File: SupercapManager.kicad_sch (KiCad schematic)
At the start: 9 parts, among them J1 JST4_F, J2 XT30_F, J3 XT30_F, J4 XT30_F, J5 XT30_F, Q11 BSC059N04LS6, Q12 BSC059N04LS6

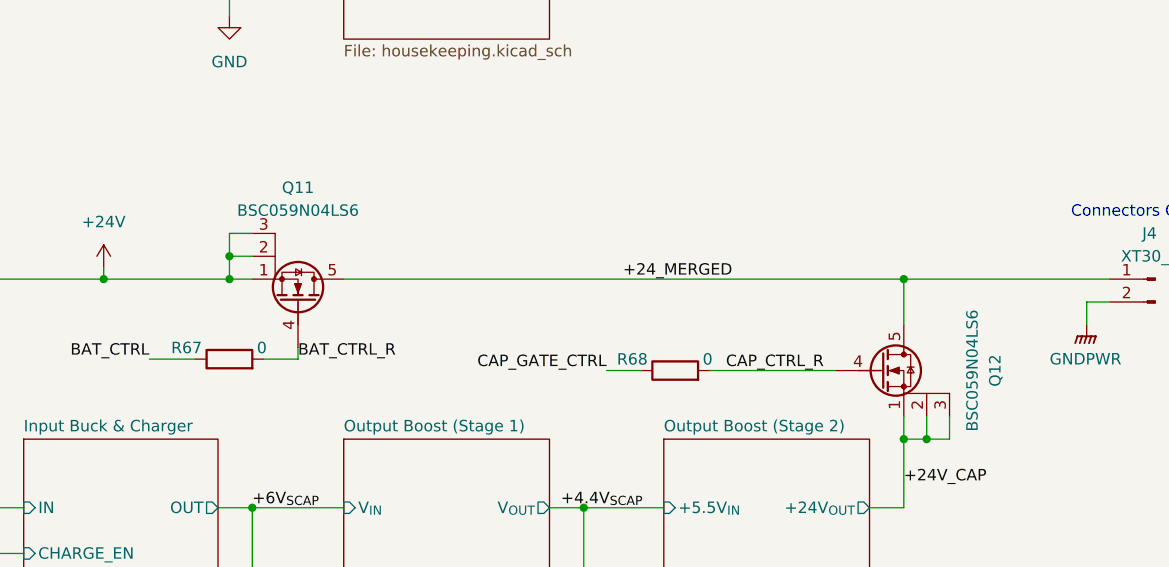
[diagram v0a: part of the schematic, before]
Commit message: Reannotate schematic
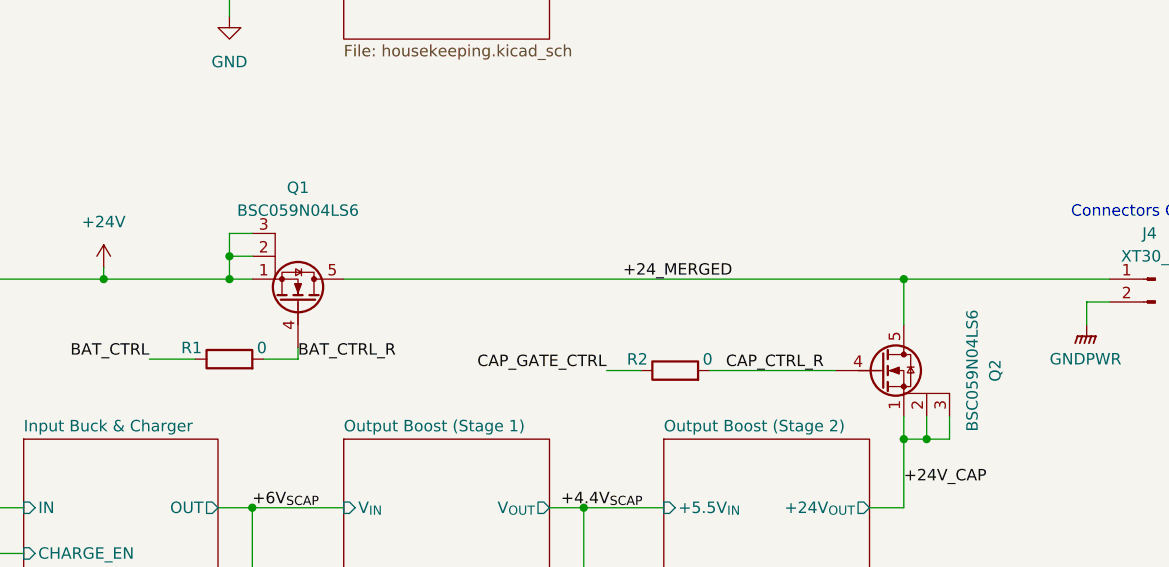
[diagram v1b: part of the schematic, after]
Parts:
- renumbered Q11 to Q1, Q12 to Q2, R67 to R1, R68 to R2
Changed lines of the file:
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@@
 		(dnp no)
 		(fields_autoplaced yes)
-		(property "Reference" "#PWR09"
+		(property "Reference" "#PWR07"
 			(at 39.37 90.17 0)
 			(effects
@@
 			(project "SupercapManager"
 				(path "/6197145b-e7d4-44cc-9d90-537b6501bf60"
-					(reference "#PWR09")
+					(reference "#PWR07")
 					(unit 1)
 				)
@@
 		(on_board yes)
 		(dnp no)
-		(property "Reference" "R68"
+		(property "Reference" "R2"
 			(at 169.672 89.662 90)
 			(effects
@@
 			(project "SupercapManager"
 				(path "/6197145b-e7d4-44cc-9d90-537b6501bf60"
-					(reference "R68")
+					(reference "R2")
 					(unit 1)
 				)
@@
 		(on_board yes)
 		(dnp no)
-		(property "Reference" "Q11"
+		(property "Reference" "Q1"
 			(at 130.81 69.85 90)
 			(effects
@@
 			(project "SupercapManager"
 				(path "/6197145b-e7d4-44cc-9d90-537b6501bf60"
-					(reference "Q11")
+					(reference "Q1")
 					(unit 1)
 				)
@@
 		(dnp no)
 		(fields_autoplaced yes)
-		(property "Reference" "#PWR04"
+		(property "Reference" "#PWR02"
 			(at 123.19 57.15 0)
 			(effects
@@
 			(project ""
 				(path "/6197145b-e7d4-44cc-9d90-537b6501bf60"
-					(reference "#PWR04")
+					(reference "#PWR02")
 					(unit 1)
 				)
@@
 		(on_board yes)
 		(dnp no)
-		(property "Reference" "R67"
+		(property "Reference" "R1"
 			(at 120.142 88.392 90)
 			(effects
@@
 			(project "SupercapManager"
 				(path "/6197145b-e7d4-44cc-9d90-537b6501bf60"
-					(reference "R67")
+					(reference "R1")
 					(unit 1)
 				)
@@
 		(dnp no)
 		(fields_autoplaced yes)
-		(property "Reference" "#PWR021"
+		(property "Reference" "#PWR012"
 			(at 241.3 116.84 0)
 			(effects
@@
 			(project "SupercapManager"
 				(path "/6197145b-e7d4-44cc-9d90-537b6501bf60"
-					(reference "#PWR021")
+					(reference "#PWR012")
 					(unit 1)
 				)
@@
 		(dnp no)
 		(fields_autoplaced yes)
-		(property "Reference" "#PWR06"
+		(property "Reference" "#PWR09"
 			(at 241.3 90.17 0)
 			(effects
@@
 			(project ""
 				(path "/6197145b-e7d4-44cc-9d90-537b6501bf60"
-					(reference "#PWR06")
+					(reference "#PWR09")
 					(unit 1)
 				)
@@
 		(dnp no)
 		(fields_autoplaced yes)
-		(property "Reference" "#PWR08"
+		(property "Reference" "#PWR010"
 			(at 241.3 99.06 0)
 			(effects
@@
 			(project ""
 				(path "/6197145b-e7d4-44cc-9d90-537b6501bf60"
-					(reference "#PWR08")
+					(reference "#PWR010")
 					(unit 1)
 				)
@@
 		(dnp no)
 		(fields_autoplaced yes)
-		(property "Reference" "#PWR010"
+		(property "Reference" "#PWR08"
 			(at 218.44 90.17 0)
 			(effects
@@
 			(project "SupercapManager"
 				(path "/6197145b-e7d4-44cc-9d90-537b6501bf60"
-					(reference "#PWR010")
+					(reference "#PWR08")
 					(unit 1)
 				)
@@
 		(dnp no)
 		(fields_autoplaced yes)
-		(property "Reference" "#PWR07"
+		(property "Reference" "#PWR06"
 			(at 109.22 82.55 0)
 			(effects
@@
 			(project ""
 				(path "/6197145b-e7d4-44cc-9d90-537b6501bf60"
-					(reference "#PWR07")
+					(reference "#PWR06")
 					(unit 1)
 				)
@@
 		(dnp no)
 		(fields_autoplaced yes)
-		(property "Reference" "#PWR014"
+		(property "Reference" "#PWR013"
 			(at 125.73 181.61 0)
 			(effects
@@
 			(project "SupercapManager"
 				(path "/6197145b-e7d4-44cc-9d90-537b6501bf60"
-					(reference "#PWR014")
+					(reference "#PWR013")
 					(unit 1)
 				)
@@
 		(on_board yes)
 		(dnp no)
-		(property "Reference" "Q12"
+		(property "Reference" "Q2"
 			(at 208.28 90.17 90)
 			(effects
@@
 			(project "SupercapManager"
 				(path "/6197145b-e7d4-44cc-9d90-537b6501bf60"
-					(reference "Q12")
+					(reference "Q2")
 					(unit 1)
 				)
@@
 		(dnp no)
 		(fields_autoplaced yes)
-		(property "Reference" "#PWR02"
+		(property "Reference" "#PWR04"
 			(at 238.76 60.96 0)
 			(effects
@@
 			(project ""
 				(path "/6197145b-e7d4-44cc-9d90-537b6501bf60"
-					(reference "#PWR02")
-					(unit 1)
-				)
+					(reference "#PWR04")
+					(unit 1)
+				)

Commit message: Finalized design !!!
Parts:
- added J9: XT30_F, Connector_AMASS:AMASS_XT30U-F_1x02_P5.0mm_Vertical, symbol Connector:Conn_01x02_Pin
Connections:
- net GNDPWR: now also J9.2 (Pin_2)
- new net +5V: J9.1 (Pin_1)
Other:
- sheet Housekeeping Power Supplies ports: added +5V_{OUT}; removed none
- sheet Output Boost (Stage 1) ports: added IN, OUT; removed V_{IN}, V_{OUT}
- sheet Output Boost (Stage 2) ports: added IN; removed +5.5V_{IN}
- note added: "+6V to Mini PC GND"
- note removed: "+6V to GNDPWR"

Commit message: Various touchups
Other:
- note added: "+5V to Mini PC GND"
- note removed: "+6V to Mini PC GND"
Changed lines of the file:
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@@
 		)
 	)
-	(text "+6V to Mini PC GND"
+	(text "+5V to Mini PC GND"
 		(exclude_from_sim no)
 		(at 245.745 110.49 0)

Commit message: Various schematic touchups
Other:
- note added: "Connector to supercap charge balancer"
- note added: "Supercapacitor host board"
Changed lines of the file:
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@@
+		)
+	)
+	(text "Supercapacitor\nhost board"
+		(exclude_from_sim no)
+		(at 182.88 129.54 0)
+		(effects
+			(font
+				(size 1.27 1.27)
+			)
 		)
 	)
@@
 			)
 			(justify top)
+		)
+	)
+	(text "Connector to supercap\ncharge balancer"
+		(exclude_from_sim no)
+		(at 180.34 46.99 0)
+		(effects
+			(font
+				(size 1.27 1.27)
+			)
+			(justify left)
 		)
 	)
@@
 	(text "Connectors to &\nfrom supercap + SCMM"
 		(exclude_from_sim no)
-		(at 131.064 182.372 0)
+		(at 137.414 172.72 0)
 		(effects
 			(font
 				(size 1.27 1.27)
 			)
-			(justify top)
+			(justify left)
 		)
 	)

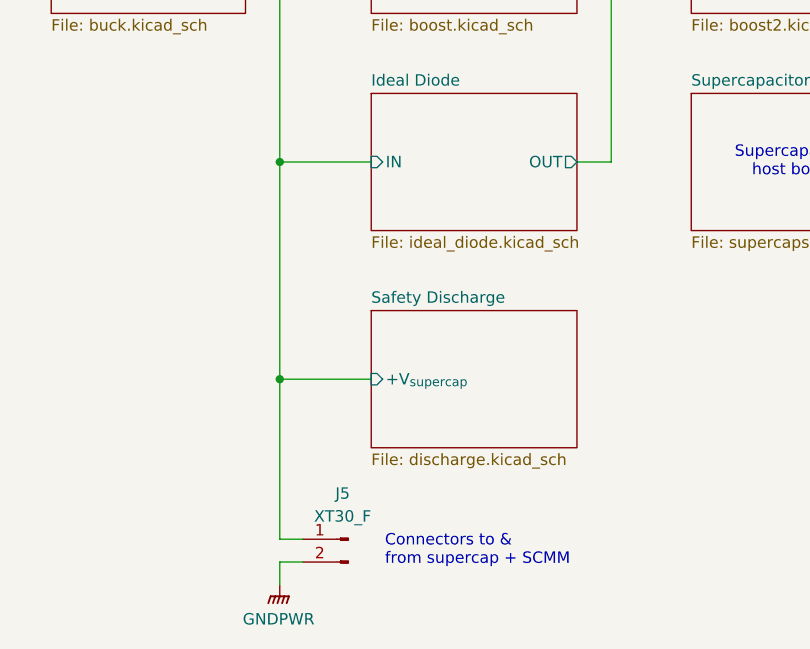
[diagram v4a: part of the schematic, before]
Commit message: Adjusted some things + changed discharge to have a smaller time constant
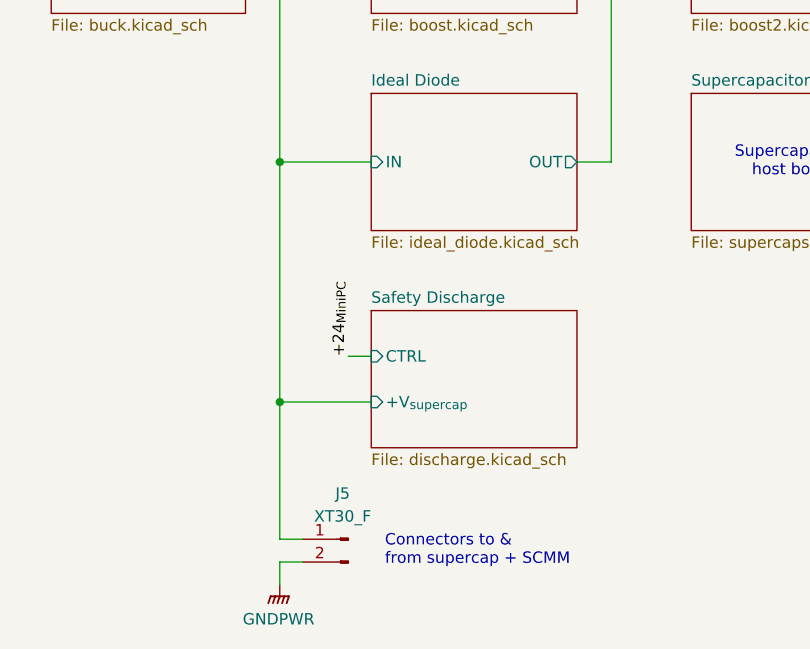
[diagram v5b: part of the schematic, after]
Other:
- sheet Safety Discharge ports: added CTRL; removed none
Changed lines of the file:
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@@
 	)
 	(junction
-		(at 125.73 153.67)
+		(at 125.73 156.21)
 		(diameter 0)
 		(color 0 0 0 0)
@@
 	(wire
 		(pts
+			(xy 125.73 156.21) (xy 125.73 171.45)
+		)
+		(stroke
+			(width 0)
+			(type default)
+		)
+	)
+	(wire
+		(pts
 			(xy 123.19 48.26) (xy 120.65 48.26)
 		)
@@
 	(wire
 		(pts
+			(xy 133.35 151.13) (xy 135.89 151.13)
+		)
+		(stroke
+			(width 0)
+			(type default)
+		)
+	)
+	(wire
+		(pts
 			(xy 95.25 80.01) (xy 109.22 80.01)
 		)
@@
 	(wire
 		(pts
-			(xy 125.73 129.54) (xy 125.73 153.67)
+			(xy 125.73 129.54) (xy 125.73 156.21)
 		)
 		(stroke
@@
 	(wire
 		(pts
-			(xy 125.73 153.67) (xy 125.73 171.45)
-		)
-		(stroke
-			(width 0)
-			(type default)
-		)
-	)
-	(wire
-		(pts
 			(xy 95.25 105.41) (xy 100.33 105.41)
 		)
@@
 	(wire
 		(pts
-			(xy 125.73 153.67) (xy 135.89 153.67)
+			(xy 125.73 156.21) (xy 135.89 156.21)
 		)
 		(stroke
@@
 	)
 	(label "+24_{MiniPC}"
+		(at 133.35 151.13 90)
+		(effects
+			(font
+				(size 1.27 1.27)
+			)
+			(justify left bottom)
+		)
+	)
+	(label "+24_{MiniPC}"
 		(at 123.19 45.72 0)
 		(effects
@@
 		)
 		(pin "+V_{supercap}" input
-			(at 135.89 153.67 180)
+			(at 135.89 156.21 180)
+			(effects
+				(font
+					(size 1.27 1.27)
+				)
+				(justify left)
+			)
+		)
+		(pin "CTRL" input
+			(at 135.89 151.13 180)
 			(effects
 				(font
